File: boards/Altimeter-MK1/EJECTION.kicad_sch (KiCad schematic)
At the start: 40 parts, among them Q1 AOD442G

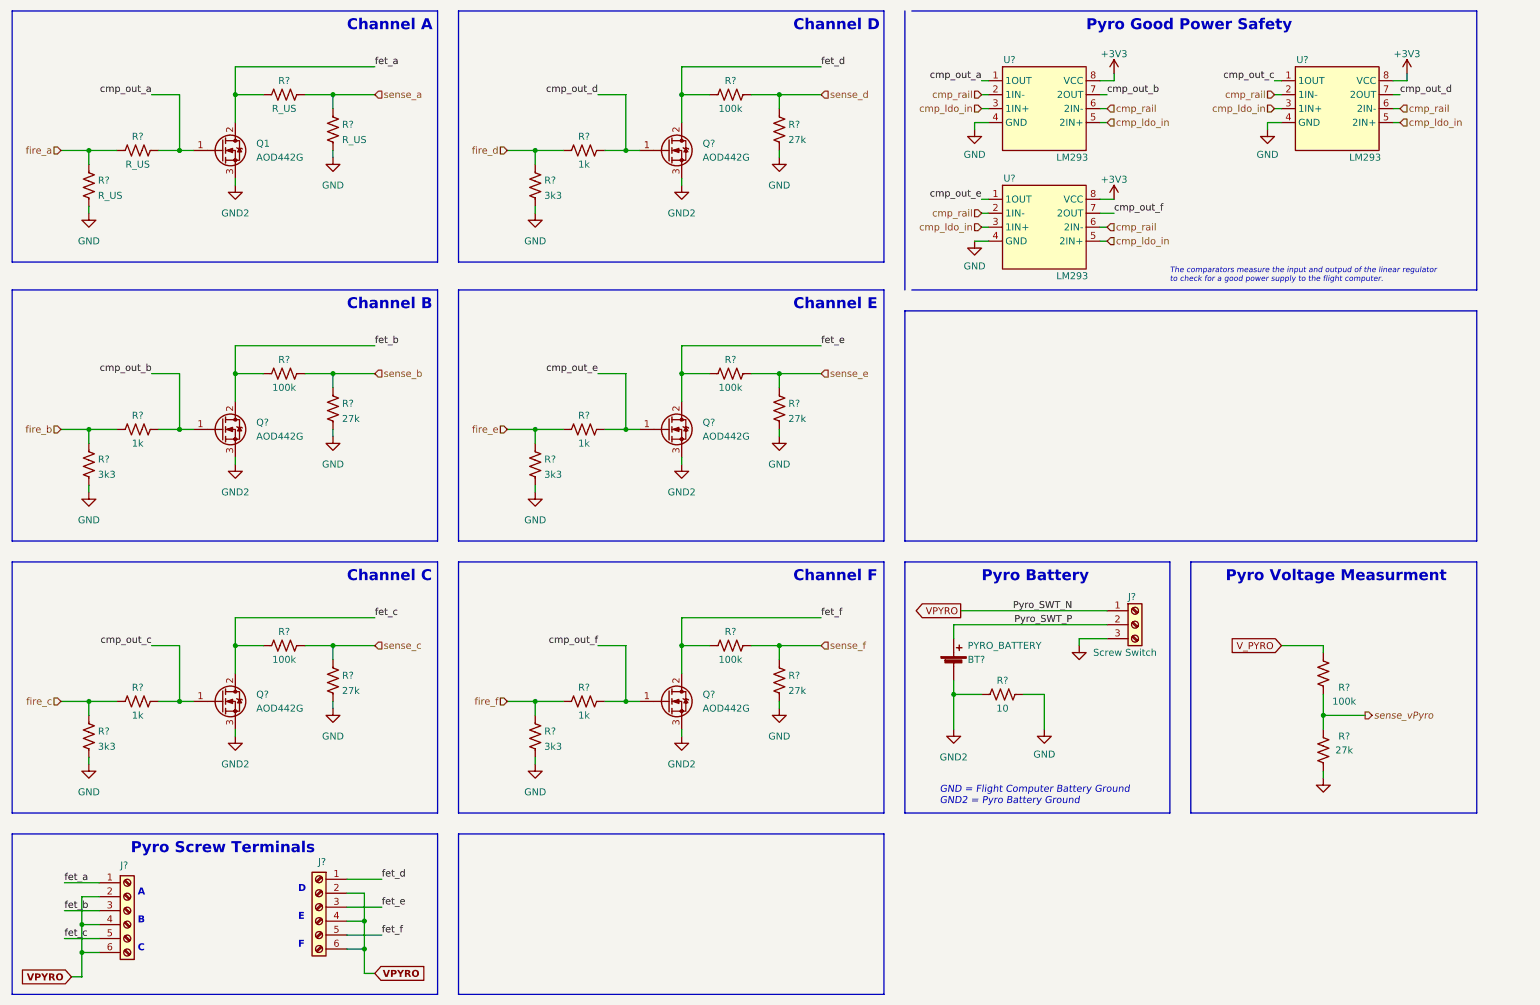
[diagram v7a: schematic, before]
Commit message: Added footprints
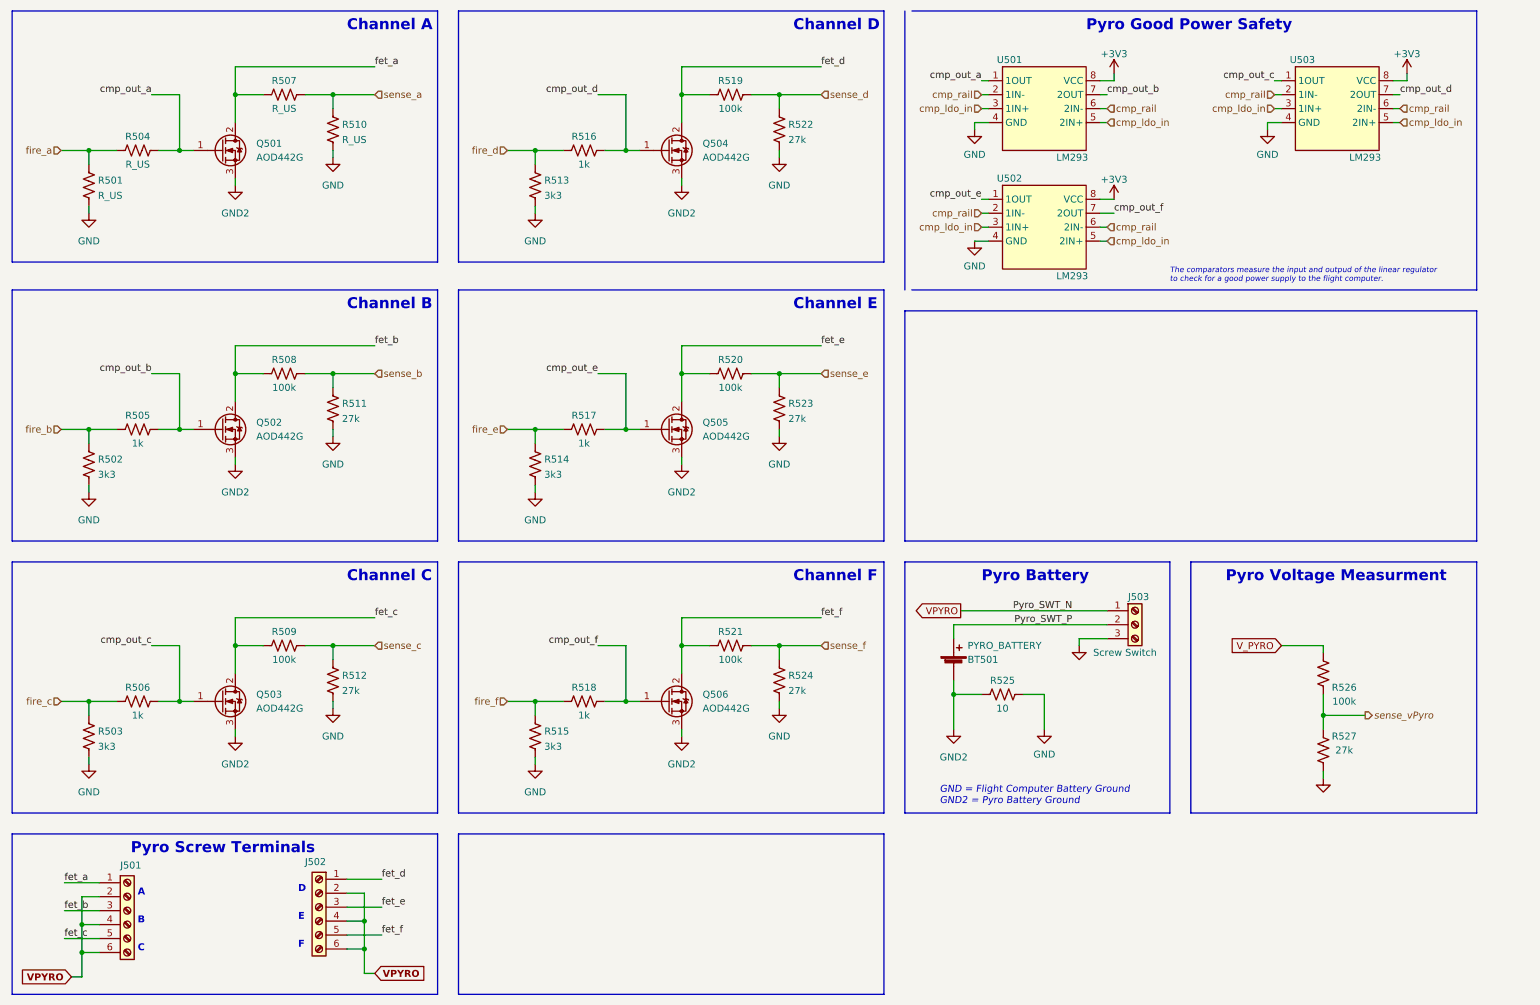
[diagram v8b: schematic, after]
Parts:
- BT501: renamed from BT?; footprint (none) -> Connector_Molex:Molex_CLIK-Mate_502443-0270_1x02-1MP_P2.00mm_Vertical
- J501, J502: renamed from J?; footprint (none) -> TerminalBlock_Phoenix:TerminalBlock_Phoenix_MKDS-1,5-6_1x06_P5.00mm_Horizontal
- J503: renamed from J?; footprint (none) -> TerminalBlock_Phoenix:TerminalBlock_Phoenix_MKDS-1,5-3_1x03_P5.00mm_Horizontal
- R501, R502, R503, R504, R505, R506, R507, R508, R509, R510, R511, R512, R513, R514, R515, R516, R517, R518, R519, R520, R521, R522, R523, R524, R525: renamed from R?; footprint Resistor_SMD:R_01005_0402Metric -> Resistor_SMD:R_0402_1005Metric
- R526, R527: renamed from R?; footprint (none) -> Resistor_SMD:R_0402_1005Metric
- U501, U502, U503: renamed from U?; footprint (none) -> Package_DFN_QFN:DFN-8-1EP_2x2mm_P0.5mm_EP0.8x1.6mm
- gave numbers to parts that had none: 5
- renumbered Q1 to Q501
